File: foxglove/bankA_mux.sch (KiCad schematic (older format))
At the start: 6 parts, among them U10 SHIFTER, U9 74HC4051

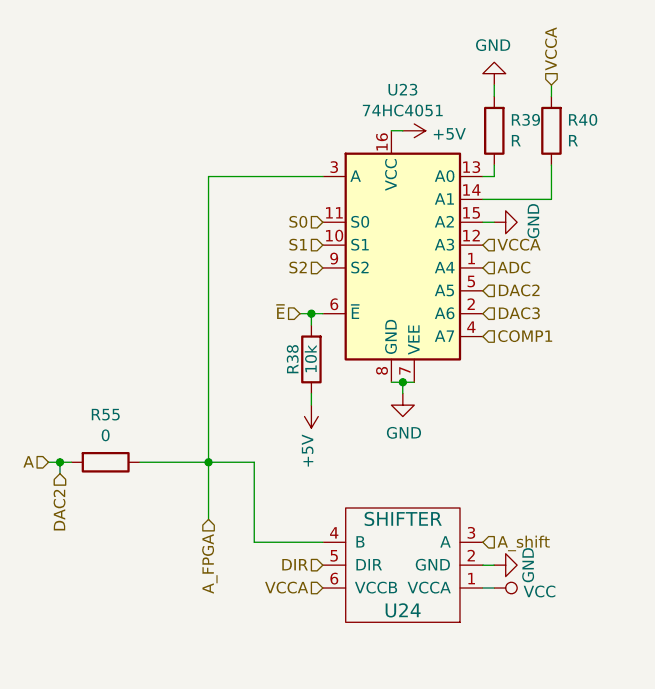
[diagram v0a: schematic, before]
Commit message: Changed DAC controlled LDO
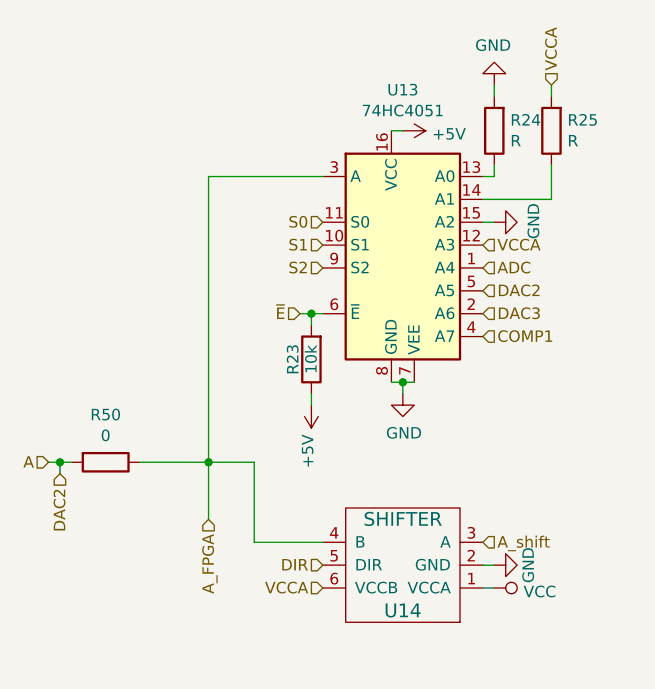
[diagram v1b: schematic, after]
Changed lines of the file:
@@
 $Descr A4 11693 8268
 encoding utf-8
-Sheet 9 9
+Sheet 4 9
 Title ""
 Date ""
@@
 AR Path="/5D1A4680/5CF3E254" Ref="U21"  Part="1"
 AR Path="/5D1A4696/5CF3E254" Ref="U23"  Part="1"
-F 0 "U23" H 4100 3428 50  0000 C CNN
+F 0 "U13" H 4100 3428 50  0000 C CNN
 F 1 "74HC4051" H 4100 3337 50  0000 C CNN
 F 2 "Package_TO_SOT_SMD:SOT-763-1" H 4050 2350 50  0001 C CNN
@@
 AR Path="/5D1A4680/5CF3E25C" Ref="#PWR0180"  Part="1"
 AR Path="/5D1A4696/5CF3E25C" Ref="#PWR0186"  Part="1"
-F 0 "#PWR0186" H 4100 2100 50  0001 C CNN
+F 0 "#PWR0156" H 4100 2100 50  0001 C CNN
 F 1 "+5V" V 4115 2378 50  0000 L CNN
 F 2 "" H 4100 2250 50  0001 C CNN
@@
 AR Path="/5D1A4680/5CF3E263" Ref="#PWR0181"  Part="1"
 AR Path="/5D1A4696/5CF3E263" Ref="#PWR0187"  Part="1"
-F 0 "#PWR0187" H 4100 3150 50  0001 C CNN
+F 0 "#PWR0157" H 4100 3150 50  0001 C CNN
 F 1 "GND" H 4105 3227 50  0000 C CNN
 F 2 "" H 4100 3400 50  0001 C CNN
@@
 AR Path="/5D1A4680/5CF3E26E" Ref="R36"  Part="1"
 AR Path="/5D1A4696/5CF3E26E" Ref="R39"  Part="1"
-F 0 "R39" H 4430 2204 50  0000 R CNN
+F 0 "R24" H 4430 2204 50  0000 R CNN
 F 1 "R" H 4430 2295 50  0000 R CNN
 F 2 "gsg-modules:0402" V 4430 2250 50  0001 C CNN
@@
 AR Path="/5D1A4680/5CF3E275" Ref="R37"  Part="1"
 AR Path="/5D1A4696/5CF3E275" Ref="R40"  Part="1"
-F 0 "R40" H 4680 2204 50  0000 R CNN
+F 0 "R25" H 4680 2204 50  0000 R CNN
 F 1 "R" H 4680 2295 50  0000 R CNN
 F 2 "gsg-modules:0402" V 4680 2250 50  0001 C CNN
@@
 AR Path="/5D1A4680/5CF3E282" Ref="#PWR0182"  Part="1"
 AR Path="/5D1A4696/5CF3E282" Ref="#PWR0188"  Part="1"
-F 0 "#PWR0188" H 4500 1800 50  0001 C CNN
+F 0 "#PWR0158" H 4500 1800 50  0001 C CNN
 F 1 "GND" H 4505 1877 50  0000 C CNN
 F 2 "" H 4500 2050 50  0001 C CNN
@@
 AR Path="/5D1A4680/5CF3E28C" Ref="U22"  Part="1"
 AR Path="/5D1A4696/5CF3E28C" Ref="U24"  Part="1"
-F 0 "U24" H 4100 4350 60  0000 C CNN
+F 0 "U14" H 4100 4350 60  0000 C CNN
 F 1 "SHIFTER" H 4100 3950 60  0000 C CNN
 F 2 "gsg-modules:SOT363" H 4100 4150 60  0001 C CNN
@@
 AR Path="/5D1A4680/5CF3E293" Ref="#PWR0183"  Part="1"
 AR Path="/5D1A4696/5CF3E293" Ref="#PWR0189"  Part="1"
-F 0 "#PWR0189" H 4500 3900 50  0001 C CNN
+F 0 "#PWR0159" H 4500 3900 50  0001 C CNN
 F 1 "GND" H 4500 4000 50  0000 C CNN
 F 2 "" H 4500 4150 60  0000 C CNN
@@
 AR Path="/5D1A4680/5CF3E2A6" Ref="R35"  Part="1"
 AR Path="/5D1A4696/5CF3E2A6" Ref="R38"  Part="1"
-F 0 "R38" V 3780 3250 50  0000 C CNN
+F 0 "R23" V 3780 3250 50  0000 C CNN
 F 1 "10k" V 3700 3250 50  0000 C CNN
 F 2 "gsg-modules:0402" V 3630 3250 50  0001 C CNN
@@
 AR Path="/5D1A4680/5CF3E2B2" Ref="#PWR0184"  Part="1"
 AR Path="/5D1A4696/5CF3E2B2" Ref="#PWR0190"  Part="1"
-F 0 "#PWR0190" H 3700 3300 50  0001 C CNN
+F 0 "#PWR0160" H 3700 3300 50  0001 C CNN
 F 1 "+5V" V 3715 3578 50  0000 L CNN
 F 2 "" H 3700 3450 50  0001 C CNN
@@
 AR Path="/5D1A4680/5CF3E2B8" Ref="#PWR0185"  Part="1"
 AR Path="/5D1A4696/5CF3E2B8" Ref="#PWR0191"  Part="1"
-F 0 "#PWR0191" H 4500 4100 50  0001 C CNN
+F 0 "#PWR0161" H 4500 4100 50  0001 C CNN
 F 1 "VCC" V 4517 4378 50  0000 L CNN
 F 2 "" H 4500 4250 50  0001 C CNN
@@
 AR Path="/5D190D22/5CB0C423" Ref="R51"  Part="1"
 AR Path="/5D1A466A/5CB0C423" Ref="R53"  Part="1"
-F 0 "R55" V 2593 3700 50  0000 C CNN
+F 0 "R50" V 2593 3700 50  0000 C CNN
 F 1 "0" V 2684 3700 50  0000 C CNN
 F 2 "gsg-modules:0402" V 2730 3700 50  0001 C CNN
@@
 AR Path="/5D1A4680/5CCD056F" Ref="#PWR0238"  Part="1"
 AR Path="/5D1A4696/5CCD056F" Ref="#PWR0239"  Part="1"
-F 0 "#PWR0239" H 4500 2400 50  0001 C CNN
+F 0 "#PWR0234" H 4500 2400 50  0001 C CNN
 F 1 "GND" H 4505 2477 50  0000 C CNN
 F 2 "" H 4500 2650 50  0001 C CNN

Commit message: Added design notes
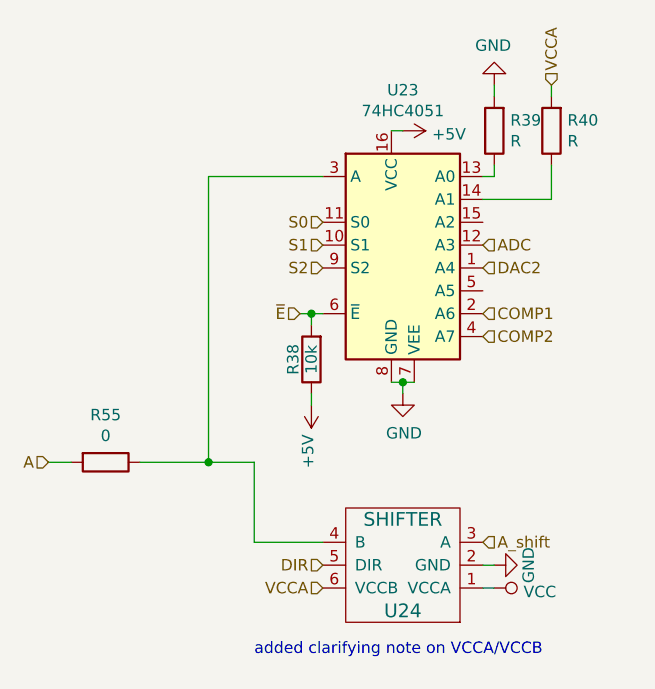
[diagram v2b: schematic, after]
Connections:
- net DAC3 is gone; now on net COMP1: U9.2 (A6)
- net A: no longer U9.5 (A5)
- net ADC: now also U9.12 (A3); no longer U9.1 (A4)
- net COMP1: no longer U9.4 (A7)
- net GND: no longer U9.15 (A2)
- net VCCA: no longer U9.12 (A3)
- net A_FPGA: no longer names the net of R48.1, U10.4 (B), U9.3 (A)
- new net COMP2: U9.4 (A7)
- new net DAC2: U9.1 (A4)
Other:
- note added: "added clarifying note on VCCA/VCCB"
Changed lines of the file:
@@
 $Descr A4 11693 8268
 encoding utf-8
-Sheet 4 9
+Sheet 9 9
 Title ""
 Date ""
@@
 AR Path="/5D1A4680/5CF3E254" Ref="U21"  Part="1"
 AR Path="/5D1A4696/5CF3E254" Ref="U23"  Part="1"
-F 0 "U13" H 4100 3428 50  0000 C CNN
+F 0 "U23" H 4100 3428 50  0000 C CNN
 F 1 "74HC4051" H 4100 3337 50  0000 C CNN
 F 2 "Package_TO_SOT_SMD:SOT-763-1" H 4050 2350 50  0001 C CNN
@@
 AR Path="/5D1A4680/5CF3E25C" Ref="#PWR0180"  Part="1"
 AR Path="/5D1A4696/5CF3E25C" Ref="#PWR0186"  Part="1"
-F 0 "#PWR0156" H 4100 2100 50  0001 C CNN
+F 0 "#PWR0186" H 4100 2100 50  0001 C CNN
 F 1 "+5V" V 4115 2378 50  0000 L CNN
 F 2 "" H 4100 2250 50  0001 C CNN
@@
 AR Path="/5D1A4680/5CF3E263" Ref="#PWR0181"  Part="1"
 AR Path="/5D1A4696/5CF3E263" Ref="#PWR0187"  Part="1"
-F 0 "#PWR0157" H 4100 3150 50  0001 C CNN
+F 0 "#PWR0187" H 4100 3150 50  0001 C CNN
 F 1 "GND" H 4105 3227 50  0000 C CNN
 F 2 "" H 4100 3400 50  0001 C CNN
@@
 AR Path="/5D1A4680/5CF3E26E" Ref="R36"  Part="1"
 AR Path="/5D1A4696/5CF3E26E" Ref="R39"  Part="1"
-F 0 "R24" H 4430 2204 50  0000 R CNN
+F 0 "R39" H 4430 2204 50  0000 R CNN
 F 1 "R" H 4430 2295 50  0000 R CNN
 F 2 "gsg-modules:0402" V 4430 2250 50  0001 C CNN
@@
 AR Path="/5D1A4680/5CF3E275" Ref="R37"  Part="1"
 AR Path="/5D1A4696/5CF3E275" Ref="R40"  Part="1"
-F 0 "R25" H 4680 2204 50  0000 R CNN
+F 0 "R40" H 4680 2204 50  0000 R CNN
 F 1 "R" H 4680 2295 50  0000 R CNN
 F 2 "gsg-modules:0402" V 4680 2250 50  0001 C CNN
@@
 AR Path="/5D1A4680/5CF3E282" Ref="#PWR0182"  Part="1"
 AR Path="/5D1A4696/5CF3E282" Ref="#PWR0188"  Part="1"
-F 0 "#PWR0158" H 4500 1800 50  0001 C CNN
+F 0 "#PWR0188" H 4500 1800 50  0001 C CNN
 F 1 "GND" H 4505 1877 50  0000 C CNN
 F 2 "" H 4500 2050 50  0001 C CNN
@@
 AR Path="/5D1A4680/5CF3E28C" Ref="U22"  Part="1"
 AR Path="/5D1A4696/5CF3E28C" Ref="U24"  Part="1"
-F 0 "U14" H 4100 4350 60  0000 C CNN
+F 0 "U24" H 4100 4350 60  0000 C CNN
 F 1 "SHIFTER" H 4100 3950 60  0000 C CNN
 F 2 "gsg-modules:SOT363" H 4100 4150 60  0001 C CNN
@@
 AR Path="/5D1A4680/5CF3E293" Ref="#PWR0183"  Part="1"
 AR Path="/5D1A4696/5CF3E293" Ref="#PWR0189"  Part="1"
-F 0 "#PWR0159" H 4500 3900 50  0001 C CNN
+F 0 "#PWR0189" H 4500 3900 50  0001 C CNN
 F 1 "GND" H 4500 4000 50  0000 C CNN
 F 2 "" H 4500 4150 60  0000 C CNN
@@
 AR Path="/5D1A4680/5CF3E2A6" Ref="R35"  Part="1"
 AR Path="/5D1A4696/5CF3E2A6" Ref="R38"  Part="1"
-F 0 "R23" V 3780 3250 50  0000 C CNN
+F 0 "R38" V 3780 3250 50  0000 C CNN
 F 1 "10k" V 3700 3250 50  0000 C CNN
 F 2 "gsg-modules:0402" V 3630 3250 50  0001 C CNN
@@
 AR Path="/5D1A4680/5CF3E2B2" Ref="#PWR0184"  Part="1"
 AR Path="/5D1A4696/5CF3E2B2" Ref="#PWR0190"  Part="1"
-F 0 "#PWR0160" H 3700 3300 50  0001 C CNN
+F 0 "#PWR0190" H 3700 3300 50  0001 C CNN
 F 1 "+5V" V 3715 3578 50  0000 L CNN
 F 2 "" H 3700 3450 50  0001 C CNN
@@
 AR Path="/5D1A4680/5CF3E2B8" Ref="#PWR0185"  Part="1"
 AR Path="/5D1A4696/5CF3E2B8" Ref="#PWR0191"  Part="1"
-F 0 "#PWR0161" H 4500 4100 50  0001 C CNN
+F 0 "#PWR0191" H 4500 4100 50  0001 C CNN
 F 1 "VCC" V 4517 4378 50  0000 L CNN
 F 2 "" H 4500 4250 50  0001 C CNN
@@
 Text HLabel 4450 4050 2    50   Input ~ 0
 A_shift
+Text HLabel 4450 2750 2    50   Input ~ 0
+ADC
 Text HLabel 4450 2850 2    50   Input ~ 0
-ADC
-Text HLabel 4450 2950 2    50   Input ~ 0
 DAC2
 Text HLabel 4450 3050 2    50   Input ~ 0
-DAC3
-Text HLabel 4450 3150 2    50   Input ~ 0
 COMP1
 $Comp
@@
 AR Path="/5D190D22/5CB0C423" Ref="R51"  Part="1"
 AR Path="/5D1A466A/5CB0C423" Ref="R53"  Part="1"
-F 0 "R50" V 2593 3700 50  0000 C CNN
+F 0 "R55" V 2593 3700 50  0000 C CNN
 F 1 "0" V 2684 3700 50  0000 C CNN
 F 2 "gsg-modules:0402" V 2730 3700 50  0001 C CNN
@@
 	0    1    1    0
 $EndComp
-Text HLabel 3250 3950 3    50   Input ~ 0
-A_FPGA
 Wire Wire Line
 	3250 3700 3250 2450
@@
 Connection ~ 3250 3700
 Wire Wire Line
-	3250 3700 3250 3950
-Wire Wire Line
-	2550 3700 2600 3700
-Wire Wire Line
-	2600 3700 2600 3750
-Connection ~ 2600 3700
-Wire Wire Line
-	2600 3700 2650 3700
-Text HLabel 2600 3750 3    50   Input ~ 0
-DAC2
-Wire Wire Line
 	2950 3700 3250 3700
-$Comp
-L power:GND #PWR?
-U 1 1 5CCD056F
-P 4500 2650
-AR Path="/5C7E37E4/5CCD056F" Ref="#PWR?"  Part="1"
-AR Path="/5C7E37E4/5CF37D46/5CCD056F" Ref="#PWR?"  Part="1"
-AR Path="/5CF421CD/5CCD056F" Ref="#PWR0232"  Part="1"
-AR Path="/5D17D622/5CCD056F" Ref="#PWR0233"  Part="1"
-AR Path="/5D190D0C/5CCD056F" Ref="#PWR0234"  Part="1"
-AR Path="/5D190D22/5CCD056F" Ref="#PWR0235"  Part="1"
-AR Path="/5D1A4654/5CCD056F" Ref="#PWR0236"  Part="1"
-AR Path="/5D1A466A/5CCD056F" Ref="#PWR0237"  Part="1"
-AR Path="/5D1A4680/5CCD056F" Ref="#PWR0238"  Part="1"
-AR Path="/5D1A4696/5CCD056F" Ref="#PWR0239"  Part="1"
-F 0 "#PWR0234" H 4500 2400 50  0001 C CNN
-F 1 "GND" H 4505 2477 50  0000 C CNN
-F 2 "" H 4500 2650 50  0001 C CNN
-F 3 "" H 4500 2650 50  0001 C CNN
-	1    4500 2650
-	0    -1   -1   0
-$EndComp
-Text HLabel 4450 2750 2    50   Input ~ 0
-VCCA
-Wire Wire Line
-	4450 2650 4500 2650
+Text Notes 3450 4550 0    50   ~ 0
+added clarifying note on VCCA/VCCB
+Text HLabel 4450 3150 2    50   Input ~ 0
+COMP2
+Wire Wire Line
+	2550 3700 2650 3700
 $EndSCHEMATC

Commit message: Connected bank B to VCCIO7 pins, switched out voltage regulators
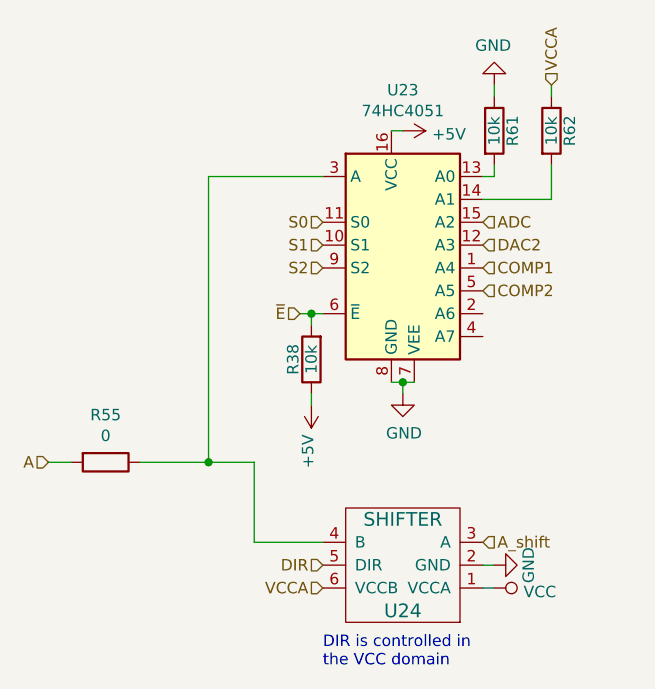
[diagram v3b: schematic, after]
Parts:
- removed R18, R19: R, gsg-modules:0402, symbol Device:R
- added R24, R25: 10k, gsg-modules:0402, symbol Device:R
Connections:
- net ADC: now also U9.15 (A2); no longer U9.12 (A3)
- net COMP1: now also U9.1 (A4); no longer U9.2 (A6)
- net COMP2: now also U9.5 (A5); no longer U9.4 (A7)
- net DAC2: now also U9.12 (A3); no longer U9.1 (A4)
- net GND: now also R24.1
- net VCCA: now also R25.1
- net at U9.13 (A0): now also R24.2
- net at U9.14 (A1): now also R25.2
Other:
- note added: "DIR is controlled in \nthe VCC domain"
- note removed: "added clarifying note on VCCA/VCCB"
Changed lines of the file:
@@
 $Descr A4 11693 8268
 encoding utf-8
-Sheet 9 9
+Sheet 3 9
 Title ""
 Date ""
@@
 Wire Wire Line
 	4100 3350 4150 3350
-$Comp
-L Device:R R?
-U 1 1 5CF3E26E
-P 4500 2250
-AR Path="/5C7E37E4/5CF3E26E" Ref="R?"  Part="1"
-AR Path="/5C7E37E4/5CF37D46/5CF3E26E" Ref="R?"  Part="1"
-AR Path="/5CF421CD/5CF3E26E" Ref="R18"  Part="1"
-AR Path="/5D17D622/5CF3E26E" Ref="R21"  Part="1"
-AR Path="/5D190D0C/5CF3E26E" Ref="R24"  Part="1"
-AR Path="/5D190D22/5CF3E26E" Ref="R27"  Part="1"
-AR Path="/5D1A4654/5CF3E26E" Ref="R30"  Part="1"
-AR Path="/5D1A466A/5CF3E26E" Ref="R33"  Part="1"
-AR Path="/5D1A4680/5CF3E26E" Ref="R36"  Part="1"
-AR Path="/5D1A4696/5CF3E26E" Ref="R39"  Part="1"
-F 0 "R39" H 4430 2204 50  0000 R CNN
-F 1 "R" H 4430 2295 50  0000 R CNN
-F 2 "gsg-modules:0402" V 4430 2250 50  0001 C CNN
-F 3 "~" H 4500 2250 50  0001 C CNN
-	1    4500 2250
-	-1   0    0    1
-$EndComp
-$Comp
-L Device:R R?
-U 1 1 5CF3E275
-P 4750 2250
-AR Path="/5C7E37E4/5CF3E275" Ref="R?"  Part="1"
-AR Path="/5C7E37E4/5CF37D46/5CF3E275" Ref="R?"  Part="1"
-AR Path="/5CF421CD/5CF3E275" Ref="R19"  Part="1"
-AR Path="/5D17D622/5CF3E275" Ref="R22"  Part="1"
-AR Path="/5D190D0C/5CF3E275" Ref="R25"  Part="1"
-AR Path="/5D190D22/5CF3E275" Ref="R28"  Part="1"
-AR Path="/5D1A4654/5CF3E275" Ref="R31"  Part="1"
-AR Path="/5D1A466A/5CF3E275" Ref="R34"  Part="1"
-AR Path="/5D1A4680/5CF3E275" Ref="R37"  Part="1"
-AR Path="/5D1A4696/5CF3E275" Ref="R40"  Part="1"
-F 0 "R40" H 4680 2204 50  0000 R CNN
-F 1 "R" H 4680 2295 50  0000 R CNN
-F 2 "gsg-modules:0402" V 4680 2250 50  0001 C CNN
-F 3 "~" H 4750 2250 50  0001 C CNN
-	1    4750 2250
-	-1   0    0    1
-$EndComp
 Wire Wire Line
 	4450 2450 4500 2450
@@
 Text HLabel 4450 4050 2    50   Input ~ 0
 A_shift
+Text HLabel 4450 2650 2    50   Input ~ 0
+ADC
 Text HLabel 4450 2750 2    50   Input ~ 0
-ADC
+DAC2
 Text HLabel 4450 2850 2    50   Input ~ 0
-DAC2
-Text HLabel 4450 3050 2    50   Input ~ 0
 COMP1
 $Comp
@@
 Wire Wire Line
 	2950 3700 3250 3700
-Text Notes 3450 4550 0    50   ~ 0
-added clarifying note on VCCA/VCCB
-Text HLabel 4450 3150 2    50   Input ~ 0
+Text Notes 3750 4600 0    50   ~ 0
+DIR is controlled in \nthe VCC domain
+Text HLabel 4450 2950 2    50   Input ~ 0
 COMP2
 Wire Wire Line
 	2550 3700 2650 3700
+$Comp
+L Device:R R?
+U 1 1 5CDC112C
+P 4750 2250
+AR Path="/5CDC112C" Ref="R?"  Part="1"
+AR Path="/5C7E37E4/5CF37D46/5CDC112C" Ref="R?"  Part="1"
+AR Path="/5CF421CD/5CDC112C" Ref="R25"  Part="1"
+AR Path="/5D17D622/5CDC112C" Ref="R28"  Part="1"
+AR Path="/5D190D0C/5CDC112C" Ref="R31"  Part="1"
+AR Path="/5D190D22/5CDC112C" Ref="R34"  Part="1"
+AR Path="/5D1A4654/5CDC112C" Ref="R37"  Part="1"
+AR Path="/5D1A466A/5CDC112C" Ref="R40"  Part="1"
+AR Path="/5D1A4680/5CDC112C" Ref="R47"  Part="1"
+AR Path="/5D1A4696/5CDC112C" Ref="R62"  Part="1"
+F 0 "R62" V 4830 2250 50  0000 C CNN
+F 1 "10k" V 4750 2250 50  0000 C CNN
+F 2 "gsg-modules:0402" V 4680 2250 50  0001 C CNN
+F 3 "" H 4750 2250 50  0001 C CNN
+	1    4750 2250
+	1    0    0    -1
+$EndComp
+$Comp
+L Device:R R?
+U 1 1 5CDC1279
+P 4500 2250
+AR Path="/5CDC1279" Ref="R?"  Part="1"
+AR Path="/5C7E37E4/5CF37D46/5CDC1279" Ref="R?"  Part="1"
+AR Path="/5CF421CD/5CDC1279" Ref="R24"  Part="1"
+AR Path="/5D17D622/5CDC1279" Ref="R27"  Part="1"
+AR Path="/5D190D0C/5CDC1279" Ref="R30"  Part="1"
+AR Path="/5D190D22/5CDC1279" Ref="R33"  Part="1"
+AR Path="/5D1A4654/5CDC1279" Ref="R36"  Part="1"
+AR Path="/5D1A466A/5CDC1279" Ref="R39"  Part="1"
+AR Path="/5D1A4680/5CDC1279" Ref="R46"  Part="1"
+AR Path="/5D1A4696/5CDC1279" Ref="R61"  Part="1"
+F 0 "R61" V 4580 2250 50  0000 C CNN
+F 1 "10k" V 4500 2250 50  0000 C CNN
+F 2 "gsg-modules:0402" V 4430 2250 50  0001 C CNN
+F 3 "" H 4500 2250 50  0001 C CNN
+	1    4500 2250
+	1    0    0    -1
+$EndComp
 $EndSCHEMATC

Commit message: Added LDOs for DAC and VCCB
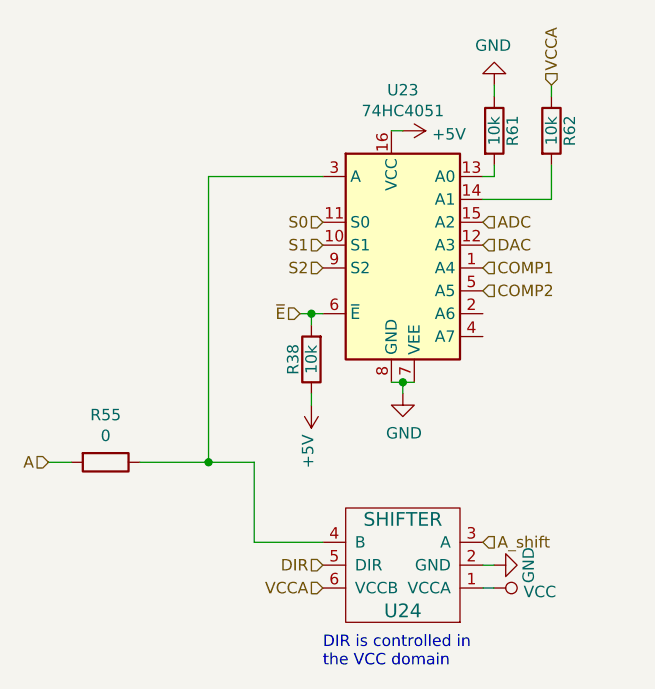
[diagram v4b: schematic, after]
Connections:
- net DAC2 renamed DAC
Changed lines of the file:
@@
 $Descr A4 11693 8268
 encoding utf-8
-Sheet 3 9
+Sheet 4 9
 Title ""
 Date ""
@@
 ADC
 Text HLabel 4450 2750 2    50   Input ~ 0
-DAC2
+DAC
 Text HLabel 4450 2850 2    50   Input ~ 0
 COMP1
